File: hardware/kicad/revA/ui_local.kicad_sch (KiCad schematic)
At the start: 0 parts

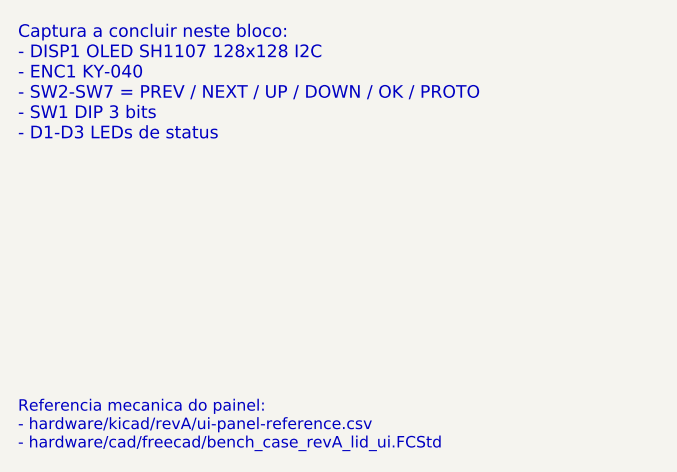
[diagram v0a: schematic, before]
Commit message: Align RevA pinout and retire legacy handoff
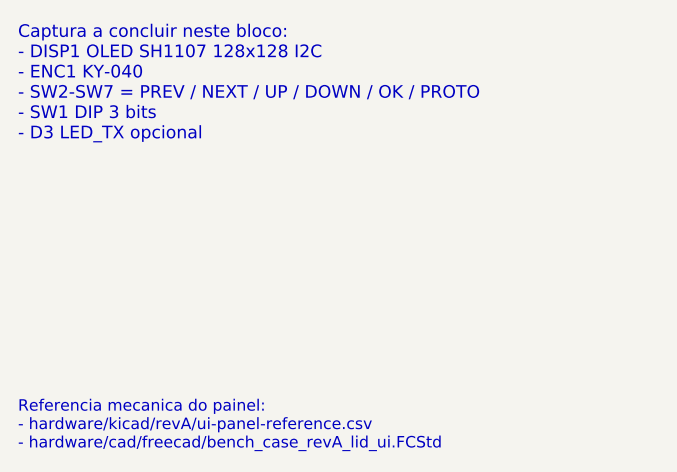
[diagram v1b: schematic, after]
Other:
- note added: "Captura a concluir neste bloco: - DISP1 OLED SH1107 128x128 I2C - ENC1 KY-040 - SW2-SW7 = PREV / NEXT / UP / DOWN / OK / PROTO - SW1 DIP 3 bits - D3 LED_TX opcional"
- note removed: "Captura a concluir neste bloco: - DISP1 OLED SH1107 128x128 I2C - ENC1 KY-040 - SW2-SW7 = PREV / NEXT / UP / DOWN / OK / PROTO - SW1 DIP 3 bits - D1-D3 LEDs de status"
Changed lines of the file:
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@@
 		(rev "A")
 		(company "You Telecom")
-		(comment 1 "SH1107 + KY-040 + 6 buttons + DIP + LEDs")
+		(comment 1 "SH1107 + KY-040 + 6 buttons + DIP + LED_TX opcional")
 	)
-	(text "Captura a concluir neste bloco:\n- DISP1 OLED SH1107 128x128 I2C\n- ENC1 KY-040\n- SW2-SW7 = PREV / NEXT / UP / DOWN / OK / PROTO\n- SW1 DIP 3 bits\n- D1-D3 LEDs de status"
+	(text "Captura a concluir neste bloco:\n- DISP1 OLED SH1107 128x128 I2C\n- ENC1 KY-040\n- SW2-SW7 = PREV / NEXT / UP / DOWN / OK / PROTO\n- SW1 DIP 3 bits\n- D3 LED_TX opcional"
 		(exclude_from_sim no)
 		(at 18 20 0)
